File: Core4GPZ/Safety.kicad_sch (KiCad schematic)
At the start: 1 part, among them U3 74LS08

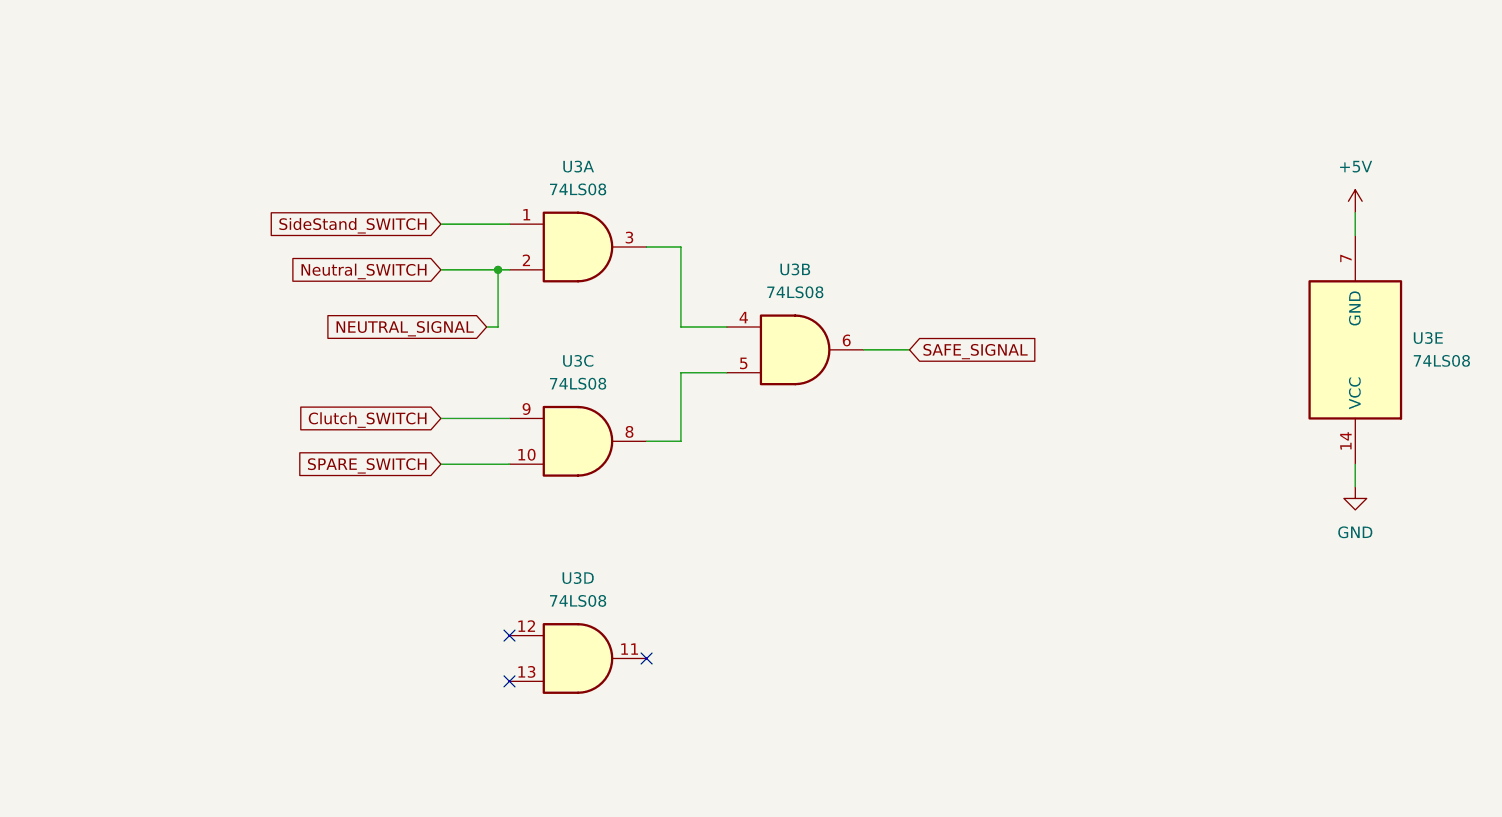
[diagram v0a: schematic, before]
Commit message: Add a splited CDI module. First Design of Ignition coil driver
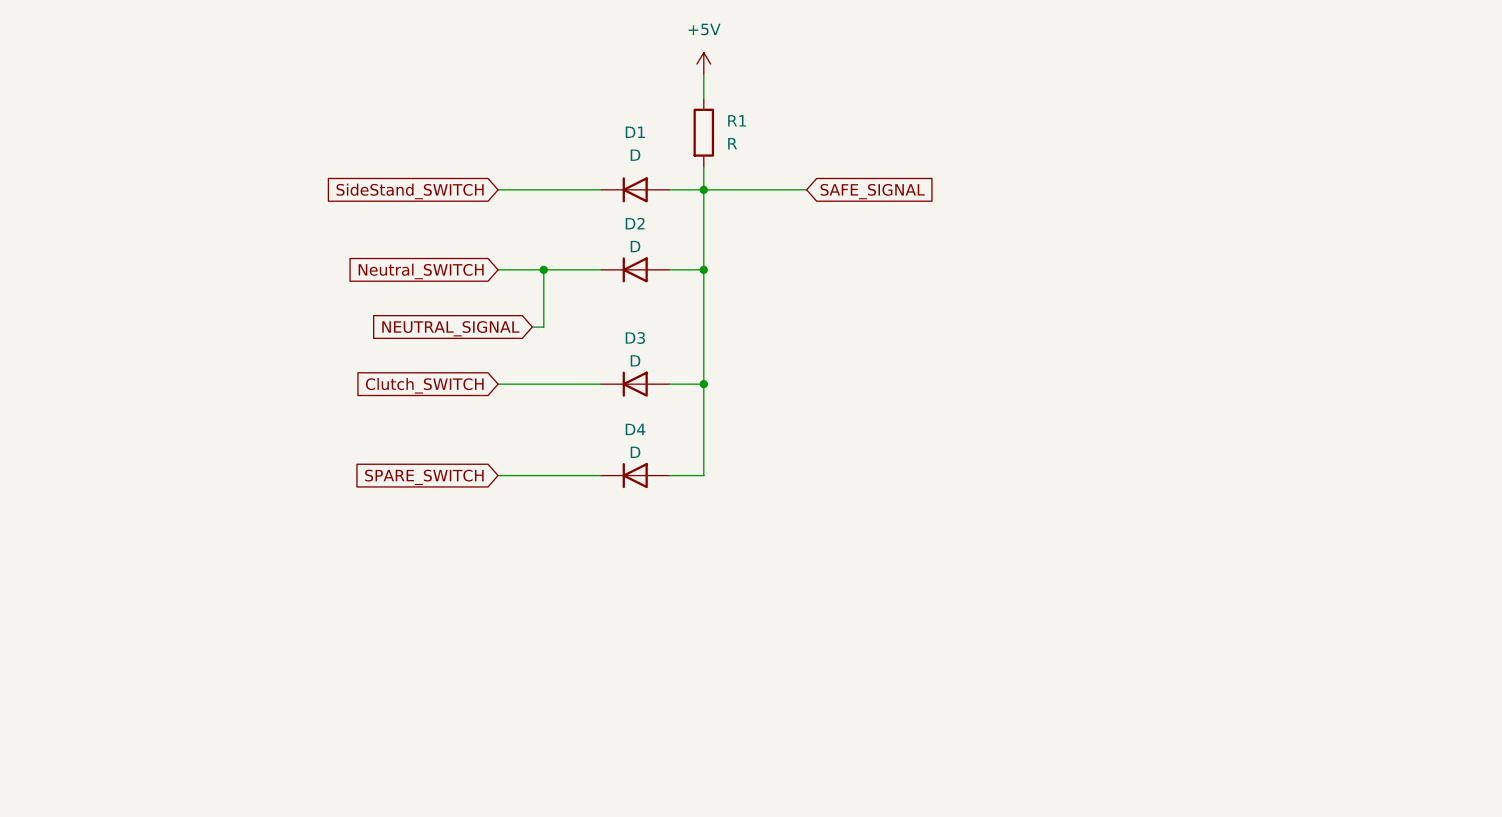
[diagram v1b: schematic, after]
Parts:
- removed U3: 74LS08, symbol 74xx:74LS08
- added D1, D2, D3, D4: D, Diode_SMD:D_0805_2012Metric_Pad1.15x1.40mm_HandSolder, symbol Device:D
- added R1: R, Resistor_SMD:R_0805_2012Metric_Pad1.20x1.40mm_HandSolder, symbol Device:R
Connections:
- net +5V: now also R1.1
- net Clutch_SWITCH: now also D3.1 (K)
- net NEUTRAL_SIGNAL: now also D2.1 (K)
- net SAFE_SIGNAL: now also D1.2 (A), D2.2 (A), D3.2 (A), D4.2 (A), R1.2
- net SPARE_SWITCH: now also D4.1 (K)
- net SideStand_SWITCH: now also D1.1 (K)
- no-connect marks 3 -> 0

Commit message: Updated security wiring and changed IGN driver for MOSFET
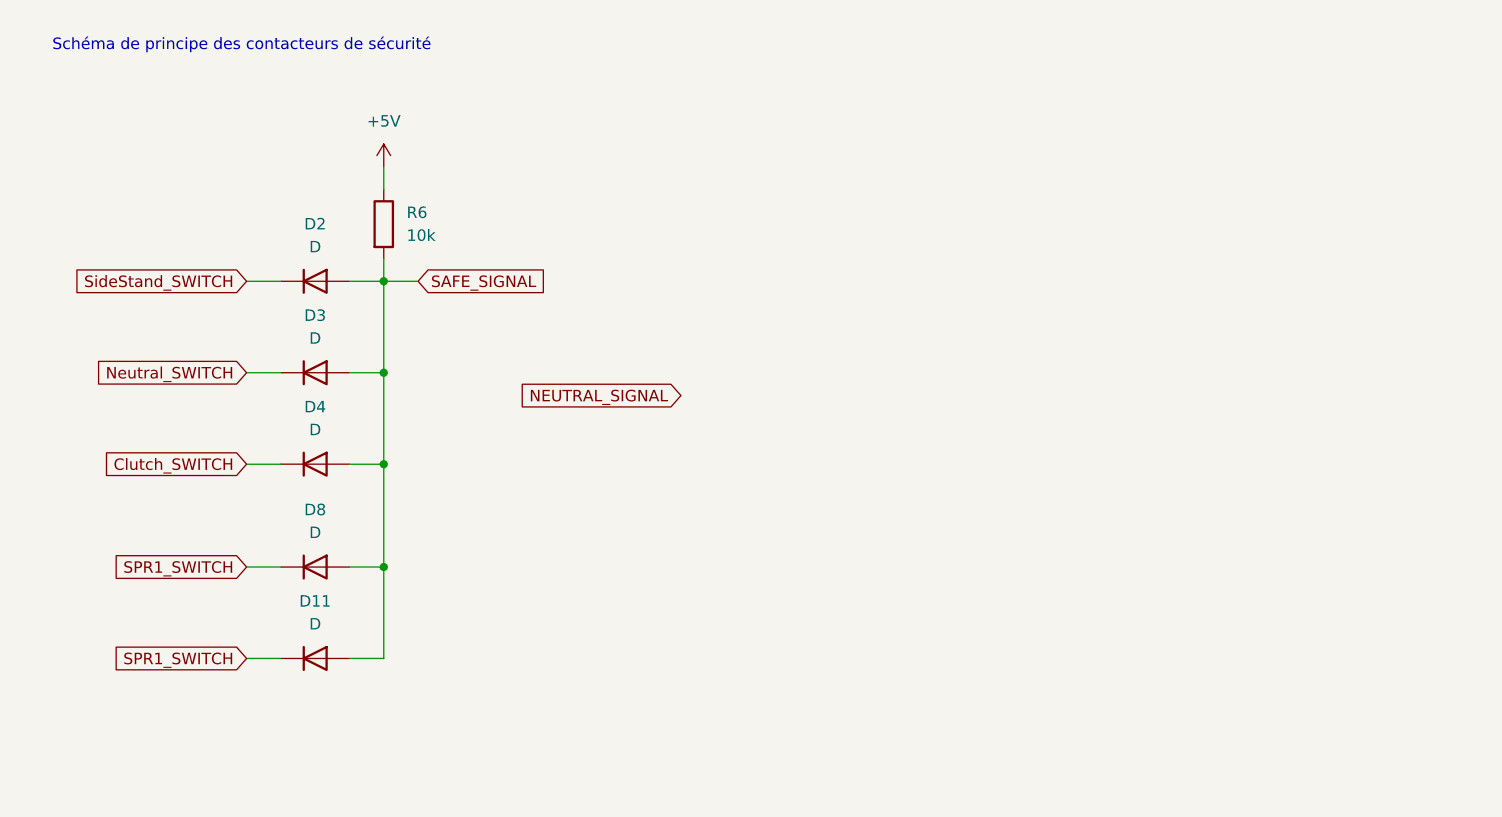
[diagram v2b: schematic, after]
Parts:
- removed D1: D, Diode_SMD:D_0805_2012Metric_Pad1.15x1.40mm_HandSolder, symbol Device:D
- removed R1: R, Resistor_SMD:R_0805_2012Metric_Pad1.20x1.40mm_HandSolder, symbol Device:R
- added D11, D8: D, Diode_SMD:D_0805_2012Metric_Pad1.15x1.40mm_HandSolder, symbol Device:D
- added R6: 10k, symbol Device:R
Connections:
- net SPARE_SWITCH is gone; now on net Clutch_SWITCH: D4.1 (K)
- net +5V: now also R6.1
- net Clutch_SWITCH: no longer D3.1 (K)
- net NEUTRAL_SIGNAL: no longer D2.1 (K)
- net SAFE_SIGNAL: now also D11.2 (A), D8.2 (A), R6.2
- net SideStand_SWITCH: now also D2.1 (K)
- new net Neutral_SWITCH: D3.1 (K)
- new net SPR1_SWITCH: D11.1 (K), D8.1 (K)
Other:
- note added: "Schéma de principe des contacteurs de sécurité"

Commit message: Test montage générateur de Haute tension
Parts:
- removed D11: D, Diode_SMD:D_0805_2012Metric_Pad1.15x1.40mm_HandSolder, symbol Device:D
- added D9: D, Diode_SMD:D_1206_3216Metric_Pad1.42x1.75mm_HandSolder, symbol Device:D
- D2, D3, D4, D8: footprint Diode_SMD:D_0805_2012Metric_Pad1.15x1.40mm_HandSolder -> Diode_SMD:D_1206_3216Metric_Pad1.42x1.75mm_HandSolder
- R6: value 10k -> 100k; footprint (none) -> Resistor_SMD:R_0805_2012Metric_Pad1.20x1.40mm_HandSolder
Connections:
- net SAFE_SIGNAL: now also D9.2 (A)
- net SPR1_SWITCH: now also D9.1 (K)
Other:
- note added: "Basically it's an OR logical gate. Based on my assumptions, the switchs on the bike are CLOSED in the UNSAFE position. In CLOSED position, they're conected to ground, and put the SAFE_SIGNAL to LOW logic level. When they're safe, the pull-up resistor set the SAFE_SIGNAL to HIGH logic level = SAFE State."

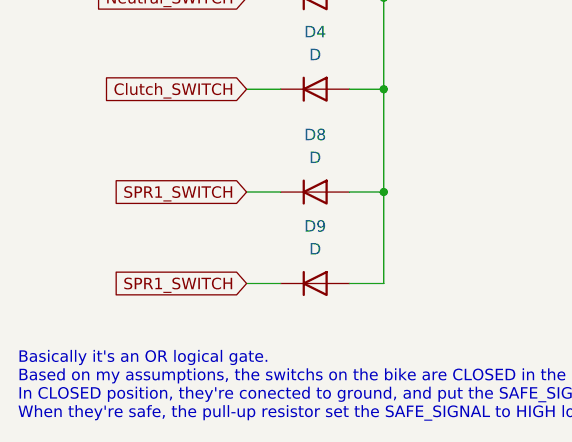
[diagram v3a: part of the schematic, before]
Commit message: Updated to Kicad 8.0
Also added Highvoltage circuit
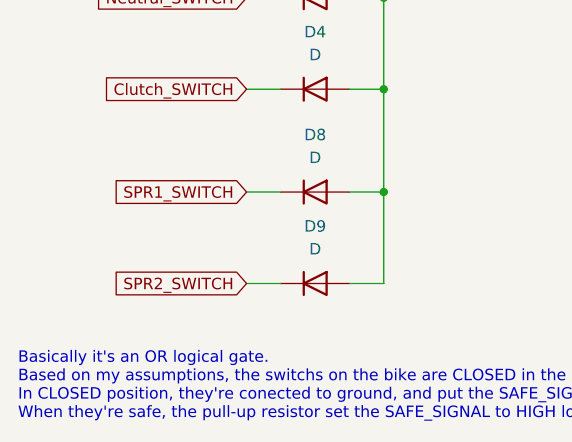
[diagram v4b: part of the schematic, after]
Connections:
- net SPR1_SWITCH: no longer D9.1 (K)
- new net SPR2_SWITCH: D9.1 (K)

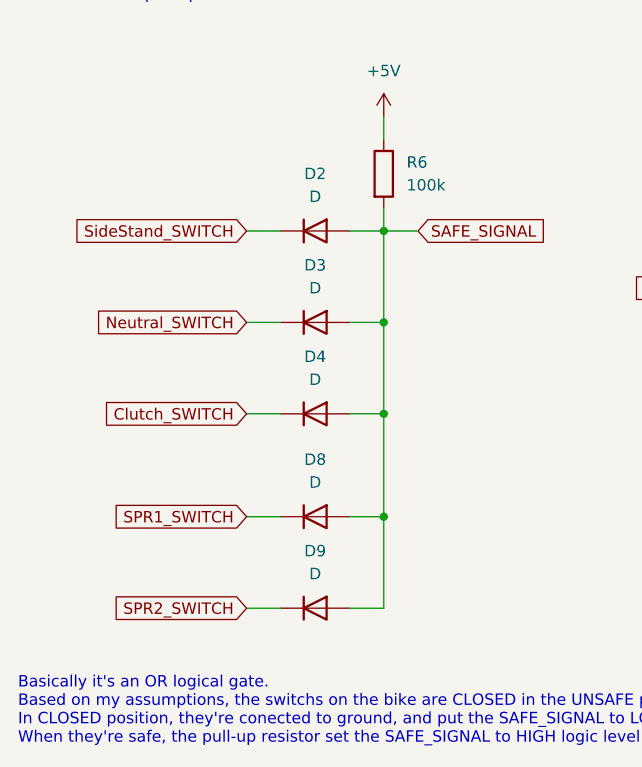
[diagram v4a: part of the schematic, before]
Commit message: Added VR Conditionner for Cam/Crank SNSR
Added some jumper for prototyping and testing purposes
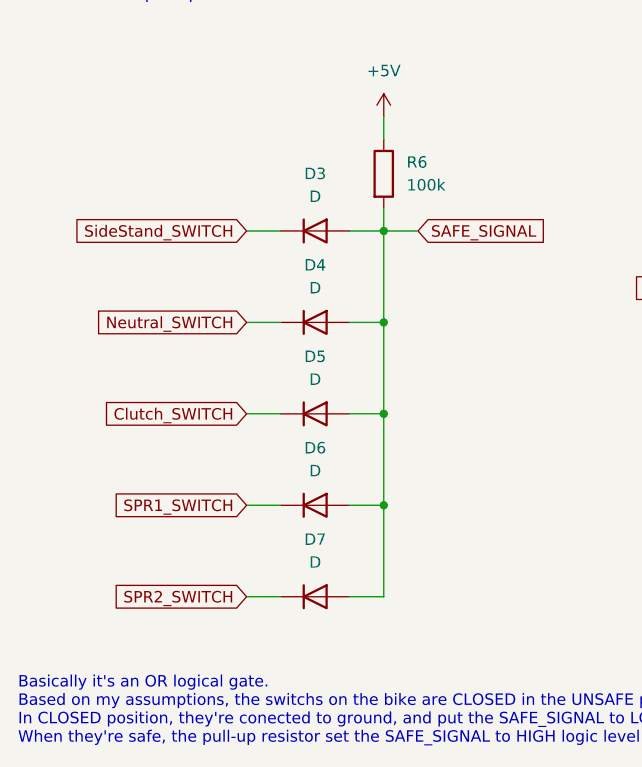
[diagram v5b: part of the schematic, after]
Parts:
- removed D3, D8, D9: D, Diode_SMD:D_1206_3216Metric_Pad1.42x1.75mm_HandSolder, symbol Device:D
- added D5, D6, D7: D, Diode_THT:D_DO-35_SOD27_P2.54mm_Vertical_KathodeUp, symbol Device:D
- D3: renamed from D2; footprint Diode_SMD:D_1206_3216Metric_Pad1.42x1.75mm_HandSolder -> Diode_THT:D_DO-35_SOD27_P2.54mm_Vertical_KathodeUp
- D4: footprint Diode_SMD:D_1206_3216Metric_Pad1.42x1.75mm_HandSolder -> Diode_THT:D_DO-35_SOD27_P2.54mm_Vertical_KathodeUp
- R6: footprint Resistor_SMD:R_0805_2012Metric_Pad1.20x1.40mm_HandSolder -> Resistor_THT:R_Axial_DIN0204_L3.6mm_D1.6mm_P5.08mm_Horizontal
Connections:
- net Clutch_SWITCH: now also D5.1 (K); no longer D4.1 (K)
- net Neutral_SWITCH: now also D4.1 (K)
- net SAFE_SIGNAL: now also D5.2 (A), D6.2 (A), D7.2 (A)
- net SPR1_SWITCH: now also D6.1 (K)
- net SPR2_SWITCH: now also D7.1 (K)
